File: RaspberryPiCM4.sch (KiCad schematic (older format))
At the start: 19 parts, among them U9 Compute_Module_4_Connectors

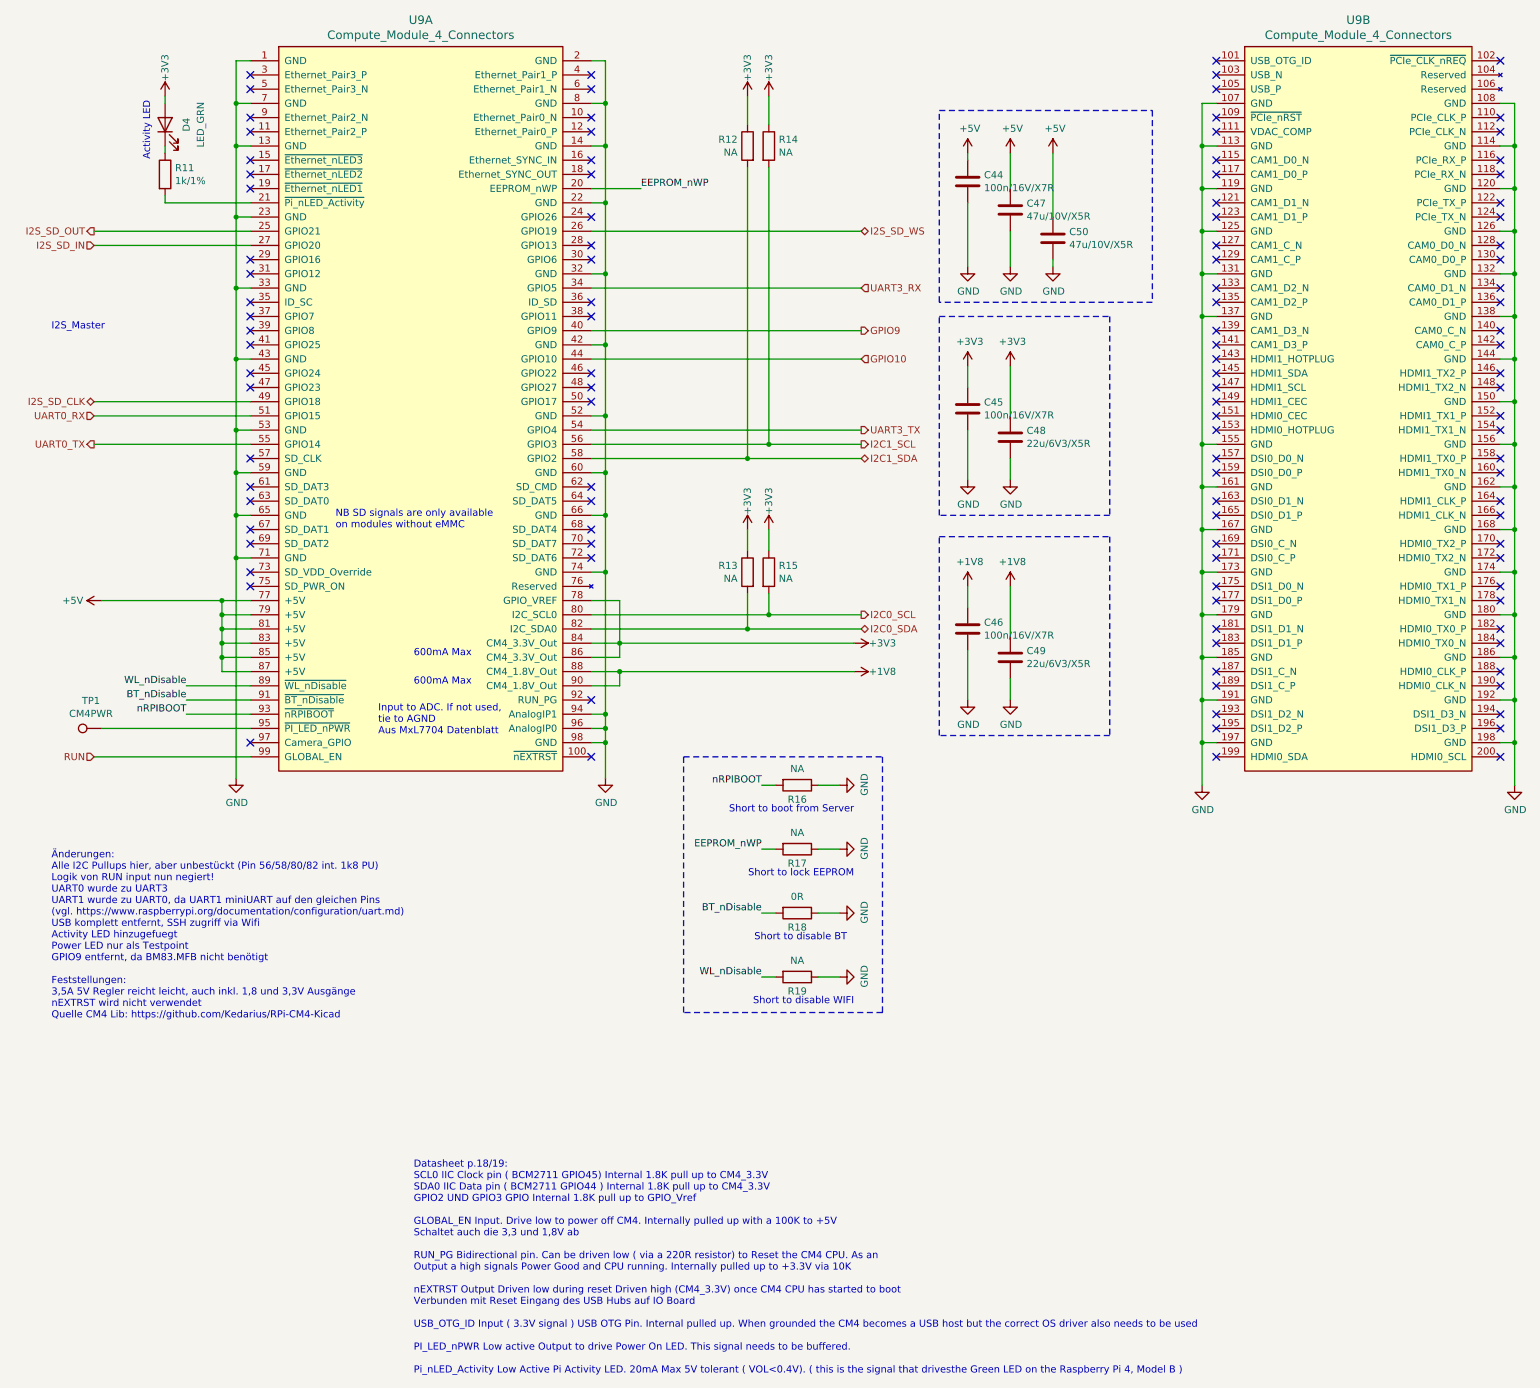
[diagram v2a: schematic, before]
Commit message: - Schaltbare BL Versorgung fertig - kleinere Value Anpassungen - Finale Annotation
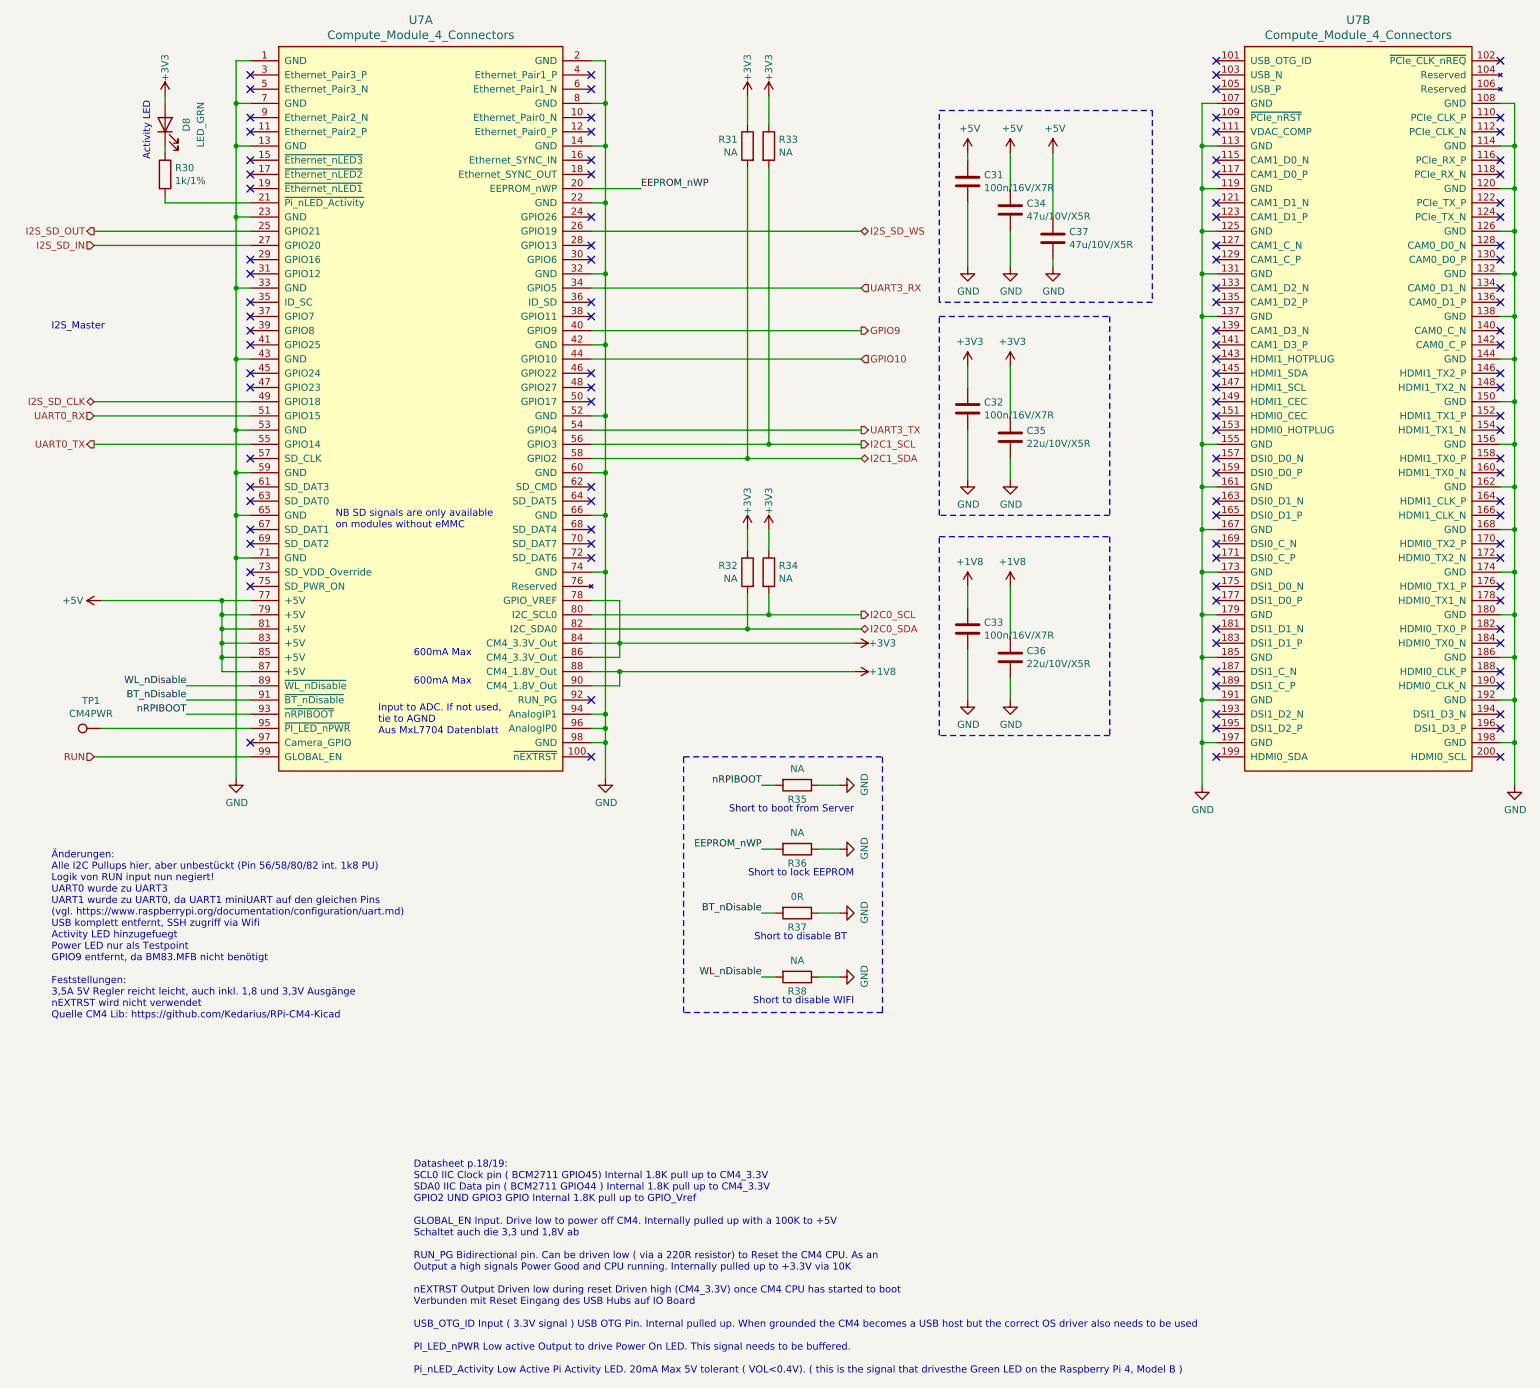
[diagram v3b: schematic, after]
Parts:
- C35: renamed from C48; value 22u/6V3/X5R -> 22u/10V/X5R
- C36: renamed from C49; value 22u/6V3/X5R -> 22u/10V/X5R
- renumbered C44 to C31, C45 to C32, C46 to C33, C47 to C34, C50 to C37, D4 to D8, R11 to R30, R12 to R31, R13 to R32, R14 to R33, R15 to R34, R16 to R35, R17 to R36, R18 to R37, R19 to R38, U9 to U7
